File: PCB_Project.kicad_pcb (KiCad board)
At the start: 8 copper layers, 61.3 x 70 mm, 222 parts, among them J1 Picoblade_CFG, J2 DF9-41P-1V32, J3 DF9-CFG-SPW1, U1 NX1H35 PBGA625, U11 AS4C8M16SA-6BIN, U12 MAX8556ETE, U13 MAX8556ETE, U14 MAX8556ETE, U15 TPS74201RGWR, U16 TPS74201RGWR, U2 CY15B108QN-40SXI, U3 CY15B108QN-40SXI, U4 CY15B108QN-40SXI, U5 AS4C8M32S-6TIN, U6 M95P32-IXMNT/E, U7 TPS3828-33DBVR, Y2 LFSPXO025225_25MHz

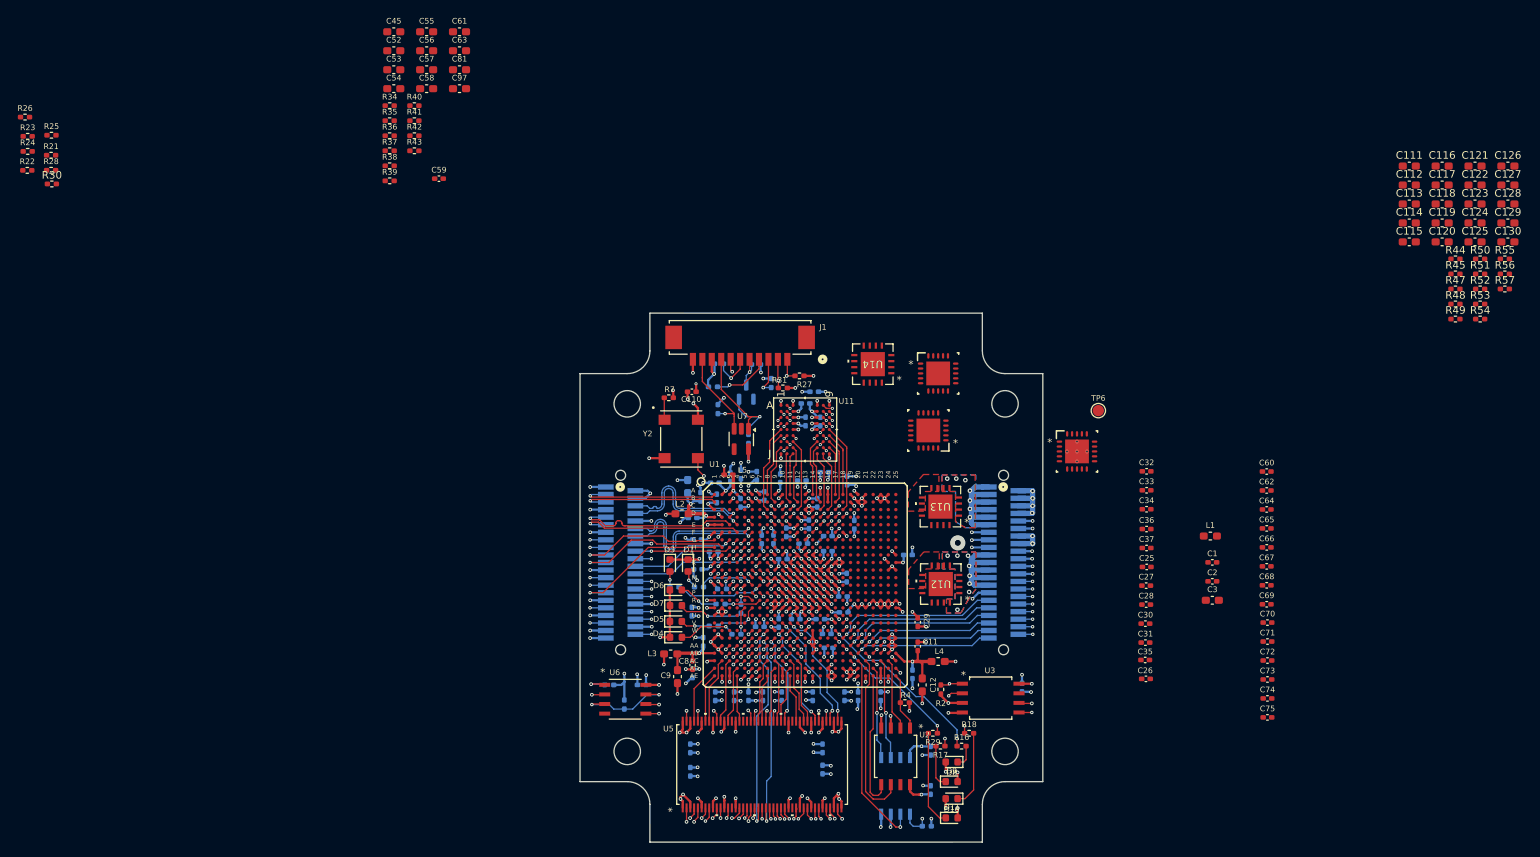
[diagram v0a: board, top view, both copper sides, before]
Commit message: finished PCB
finished power tree and power planes. Completed silkscreen placement. Added test points
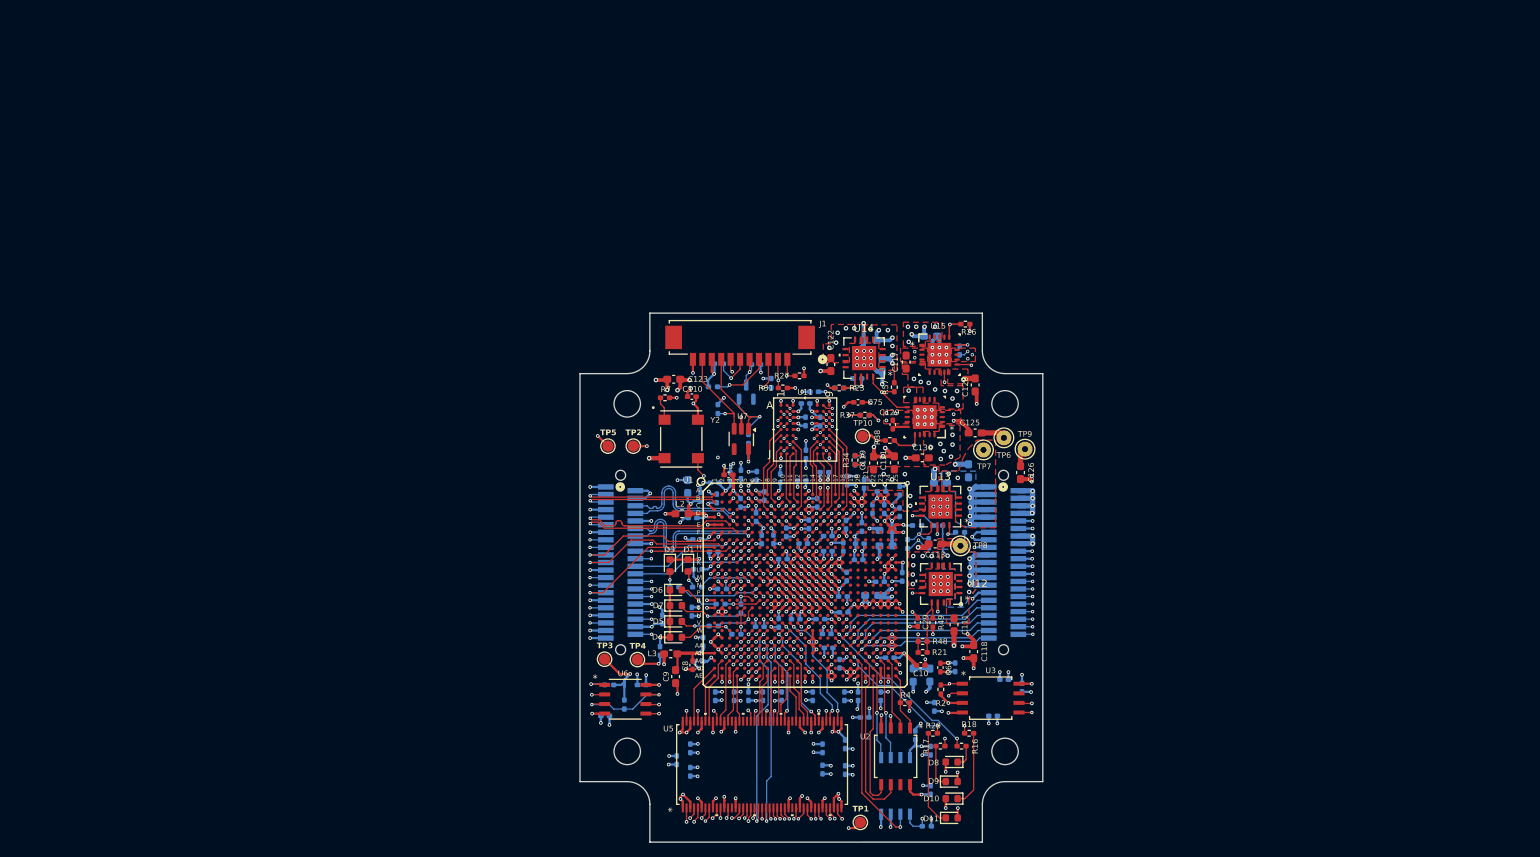
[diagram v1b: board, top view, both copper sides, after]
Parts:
- removed C45, C52, C53, C54, C55, C56, C57, C58, C61, C63, C81, C97: 10uF, Capacitor_SMD:C_0603_1608Metric_Pad1.08x0.95mm_HandSolder
- removed C59: --, Capacitor_SMD:C_0402_1005Metric_Pad0.74x0.62mm_HandSolder
- removed R28: 0 Ohm, Resistor_SMD:R_0402_1005Metric_Pad0.72x0.64mm_HandSolder
- removed R36, R39, R43: 1k, Resistor_SMD:R_0402_1005Metric_Pad0.72x0.64mm_HandSolder
- removed R40: --, Resistor_SMD:R_0402_1005Metric_Pad0.72x0.64mm_HandSolder
- removed R41: 100k, Resistor_SMD:R_0402_1005Metric_Pad0.72x0.64mm_HandSolder
- removed R42, R52: 4k02, Resistor_SMD:R_0402_1005Metric_Pad0.72x0.64mm_HandSolder
- removed R47, R55: 3k74, Resistor_SMD:R_0402_1005Metric_Pad0.72x0.64mm_HandSolder
- removed R50: 1k4, Resistor_SMD:R_0402_1005Metric_Pad0.72x0.64mm_HandSolder
- removed R54, R56: 1k2, Resistor_SMD:R_0402_1005Metric_Pad0.72x0.64mm_HandSolder
- removed the REF** at (190.8, 80.4)
- added TP1: TestPoint, DataHub_Footprints:Test_Point, F.Cu at (162.2, 129.5)
- added TP10: TestPoint, DataHub_Footprints:Test_Point, F.Cu at (162.5, 78.4)
- added TP2: TestPoint, DataHub_Footprints:Test_Point, F.Cu at (132.1, 79.7)
- added TP3: TestPoint, DataHub_Footprints:Test_Point, F.Cu at (128.3, 107.9)
- added TP4: TestPoint, DataHub_Footprints:Test_Point, F.Cu at (132.7, 107.9)
- added TP5: TestPoint, DataHub_Footprints:Test_Point, F.Cu at (128.8, 79.7)
- added TP7: TestPoint, DataHub_Footprints:PTH_pad_2x0.8, F.Cu at (178.4, 80.2)
- added TP8: TestPoint, DataHub_Footprints:PTH_pad_2x0.8, F.Cu at (175.4, 92.9)
- added TP9: TestPoint, DataHub_Footprints:PTH_pad_2x0.8, F.Cu at (183.9, 80.1)
- C1, C11, C112, C114, C115, C116, C12, C120, C124, C2, C25, C26, C27, C28, C3, C30, C31, C32, C33, C34, C35, C36, C37, C62, C64, C65, C66, C67, C68, C69, C70, C71, C72, C73, C74, L1, L4, R44, R45, R51, R53: moved to B.Cu
- C10: moved to F.Cu
- C127: footprint Capacitor_SMD:C_0603_1608Metric_Pad1.08x0.95mm_HandSolder -> Capacitor_SMD:C_0402_1005Metric_Pad0.74x0.62mm_HandSolder; moved to B.Cu
- C129: footprint Capacitor_SMD:C_0603_1608Metric_Pad1.08x0.95mm_HandSolder -> Capacitor_SMD:C_0402_1005Metric_Pad0.74x0.62mm_HandSolder
- R21, R23: value 0 Ohm -> 20k5
- R22: value 0 Ohm -> 5k; moved to B.Cu
- R24: value 0 Ohm -> 2k; moved to B.Cu
- R25: value 0 Ohm -> 4k64; moved to B.Cu
- R26: value 0 Ohm -> 1k2
- R30: value 0 Ohm -> 3k9; moved to B.Cu
- R34, R37: value 100k -> 91k
- R35: value 4k02 -> 3k9; moved to B.Cu
- R38: value 1k4 -> 1k2
- R48: value 4k02 -> 5k
- TP6: footprint TestPoint:TestPoint_Pad_D1.5mm -> DataHub_Footprints:PTH_pad_2x0.8
- moved R21 132.8 mm to (170.4, 107.0)
- moved R25 128.0 mm to (171.2, 92.5), turned to 90 degrees
- moved R24 127.5 mm to (168.4, 92.6), turned to 90 degrees
- moved R26 127.4 mm to (176.0, 63.5)
- moved R23 112.4 mm to (159.3, 72.0)
- moved R30 112.4 mm to (161.4, 81.5), turned to 90 degrees
- moved R22 111.2 mm to (159.3, 72.0)
- moved C123 108.6 mm to (137.4, 70.8)
- moved C120 88.8 mm to (163.6, 99.4), turned to 180 degrees
- moved C122 88.5 mm to (158.2, 68.9), turned to -90 degrees
- moved C74 87.7 mm to (128.3, 115.4), turned to 180 degrees
- moved C121 86.3 mm to (166.6, 81.9), turned to 90 degrees
- moved C118 85.8 mm to (177.1, 106.9), turned to -90 degrees
- moved C129 85.7 mm to (166.4, 76.8), turned to -90 degrees
- moved C111 85.5 mm to (174.5, 103.3), turned to -90 degrees
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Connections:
- C91 pad 1: VDDIO_12 -> VDD2V5
- C92 pad 1: VDDIO_12 -> VDD2V5
- C93 pad 1: VDDIO_12 -> VDD2V5
- C94 pad 1: VDDIO_12 -> VDD2V5
- C95 pad 1: VDDIO_12 -> VDD2V5
- C96 pad 1: VDDIO_12 -> VDD2V5
- R21 pad 1: VDDIO_11 -> VDD2V5A
- R21 pad 2: VDD3V3 -> Net-(U12-FB)
- R22 pad 1: VDDIO_0 -> VDD2V5
- R22 pad 2: VDD3V3 -> Net-(U14-FB)
- R23 pad 1: VDDIO_2 -> VDD2V5
- R23 pad 2: VDD3V3 -> Net-(U14-FB)
- R24 pad 1: VDDIO_3 -> CORE_VDDSEN
- R24 pad 2: VDD3V3 -> Net-(U13-FB)
- R25 pad 1: VDDIO_5 -> CORE_VDDSEN
- R25 pad 2: VDD3V3 -> Net-(U13-FB)
- R26 pad 1: VDDIO_12 -> Net-(U15-FB)
- R26 pad 2: VDD2V5 -> GND
- R30 pad 2: VDD3V3 -> Net-(U15-FB)
- R34 pad 1: +3V_IN -> VDDIO_SERVICE
- R34 pad 2: Net-(U10-EN) -> Net-(U15-FB)
- R35 pad 1: VDD2V5A -> VDD3V3
- R35 pad 2: Net-(U9-FB) -> Net-(U16-FB)
- R37 pad 1: +3V_IN -> VDD3V3
- R37 pad 2: Net-(Q1-B) -> Net-(U16-FB)
- R38 pad 1: VDD1V2 -> Net-(U16-FB)
- R38 pad 2: Net-(U10-FB) -> GND
- R57 pad 1: +3V3_IN -> /Power_Tree_LDOs/PG_LDO_SERVICE
- R57 pad 2: /Power_Tree_LDOs/PG_LDO_SERVICE -> +3V3_IN
- TP6 pad 1: (no net) -> +5V_IN
- U1 pad A2: VDDIO_12 -> VDD2V5
- U1 pad A5: VDDIO_12 -> VDD2V5
- U1 pad C1: VDDIO_12 -> VDD2V5
- U1 pad J9: VDDIO_12 -> VDD2V5
- U15 pad 13: unconnected-(U15-NC-Pad13) -> GND
- U15 pad 14: unconnected-(U15-NC-Pad14) -> GND
- U15 pad 2: unconnected-(U15-NC-Pad2) -> GND
- U15 pad 3: unconnected-(U15-NC-Pad3) -> GND
- U15 pad 4: unconnected-(U15-NC-Pad4) -> GND
- U16 pad 13: unconnected-(U16-NC-Pad13) -> GND
- U16 pad 14: unconnected-(U16-NC-Pad14) -> GND
- U16 pad 2: unconnected-(U16-NC-Pad2) -> GND
- U16 pad 3: unconnected-(U16-NC-Pad3) -> GND
- U16 pad 4: unconnected-(U16-NC-Pad4) -> GND
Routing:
- net GND: track 309.6 -> 414.0 mm, vias 210 -> 309
- net VDD2V5: track 5.65 -> 43.8 mm, vias 4 -> 20
- net Net-(U13-POK(POR)): track 0.00 -> 32.0 mm, vias 0 -> 2
- net Net-(U15-FB): track 0.00 -> 29.0 mm, vias 0 -> 2
- net CORE_VDDSEN: track 0.71 -> 27.1 mm, vias 1 -> 2
- net VDD3V3: track 94.0 -> 114.9 mm, vias 68 -> 88
- net VDD1V2: track 51.4 -> 71.3 mm, vias 37 -> 53
- net /Power_Tree_LDOs/PG_LDO_SERVICE: track 0.00 -> 18.8 mm, vias 0 -> 2
- net +3V3_IN: track 15.0 -> 33.1 mm, vias 9 -> 14
- net Net-(U16-FB): track 0.00 -> 13.7 mm, vias 0 -> 2
- net Net-(U12-POK(POR)): track 0.00 -> 13.5 mm, vias 0 -> 2
- net VDD2V5A: track 19.0 -> 31.2 mm, vias 18 -> 30
- net VDDIO_12: track 10.7 -> 0.00 mm, vias 7 -> 0
- net VDDIO_SERVICE: track 25.6 -> 36.2 mm, vias 12 -> 19
- net Net-(U12-FB): track 0.00 -> 8.12 mm
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- added copper zone on In3.Cu, net +3V3_IN
- added copper zone on F.Cu, net +3V6_IN
- added copper zone on In3.Cu, net +3V6_IN
- added copper zone on F.Cu, net +5V_IN
- added copper zone on In4.Cu, net +5V_IN
- added copper zone on F.Cu, net GND
- added copper zone on F.Cu, net VDD2V5
- added copper zone on In4.Cu, net VDD2V5
- added copper zone on F.Cu, net VDD3V3
- added copper zone on In4.Cu, net VDD3V3
- added copper zone on F.Cu, net VDDIO_SERVICE
- added copper zone on In4.Cu, net VDDIO_SERVICE

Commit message: connectors df9 distance adjusted
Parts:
- moved J3 0.11 mm to (130.5, 95.1)
- moved J2 0.07 mm to (181.0, 95.1)
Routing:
- net GND: track 414.0 -> 415.4 mm
